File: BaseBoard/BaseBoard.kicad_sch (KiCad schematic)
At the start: 43 parts, among them J1 USB_C_DEALON-USB-US31-106, J2 Serial Port, J3 base connector, Q1 PMN48XP, SW2 boot, SW3 Reset, U1 ESP32-WROOM-E, U3 MCP73831-2ACI-OT, U4 XC6210B332MR

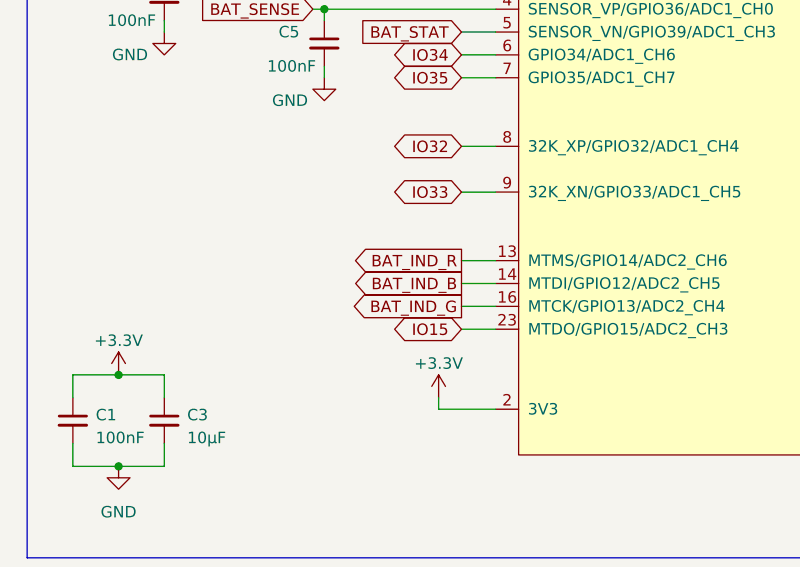
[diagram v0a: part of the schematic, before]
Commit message: Reroutes pins for the LED
After fixing the schematic symbol, we needed to reflect the changes in
the layout.
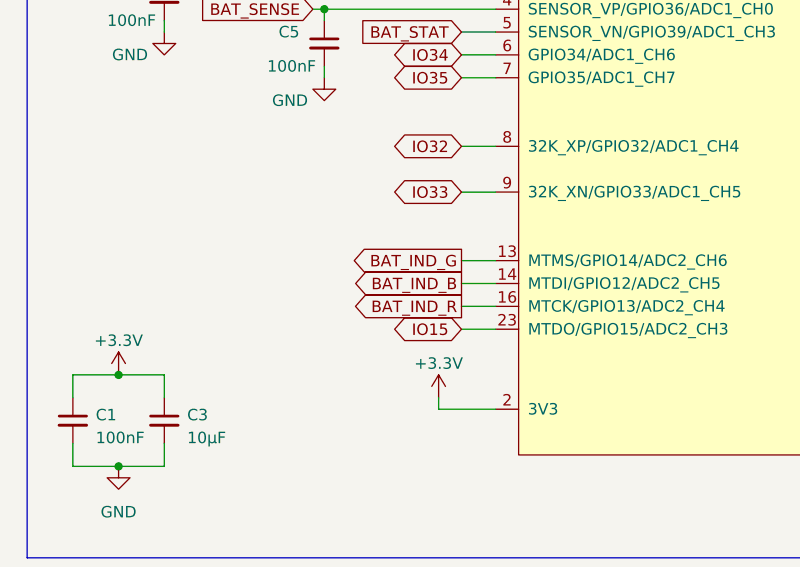
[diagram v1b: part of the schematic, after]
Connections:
- net BAT_IND_G: now also U1.13 (MTMS/GPIO14/ADC2_CH6); no longer U1.16 (MTCK/GPIO13/ADC2_CH4)
- net BAT_IND_R: now also U1.16 (MTCK/GPIO13/ADC2_CH4); no longer U1.13 (MTMS/GPIO14/ADC2_CH6)
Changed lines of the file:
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@@
     )
   )
-  (global_label "BAT_IND_R" (shape output) (at 62.23 87.63 180) (fields_autoplaced)
+  (global_label "BAT_IND_R" (shape output) (at 62.23 92.71 180) (fields_autoplaced)
     (effects (font (size 1.27 1.27)) (justify right))
-    (property "Intersheetrefs" "${INTERSHEET_REFS}" (id 0) (at 49.7463 87.63 0)
+    (property "Intersheetrefs" "${INTERSHEET_REFS}" (id 0) (at 49.7463 92.71 0)
       (effects (font (size 1.27 1.27)) (justify right) hide)
     )
@@
     )
   )
-  (global_label "BAT_IND_G" (shape output) (at 62.23 92.71 180) (fields_autoplaced)
+  (global_label "BAT_IND_G" (shape output) (at 62.23 87.63 180) (fields_autoplaced)
     (effects (font (size 1.27 1.27)) (justify right))
-    (property "Intersheetrefs" "${INTERSHEET_REFS}" (id 0) (at 49.7463 92.71 0)
+    (property "Intersheetrefs" "${INTERSHEET_REFS}" (id 0) (at 49.7463 87.63 0)
       (effects (font (size 1.27 1.27)) (justify right) hide)
     )

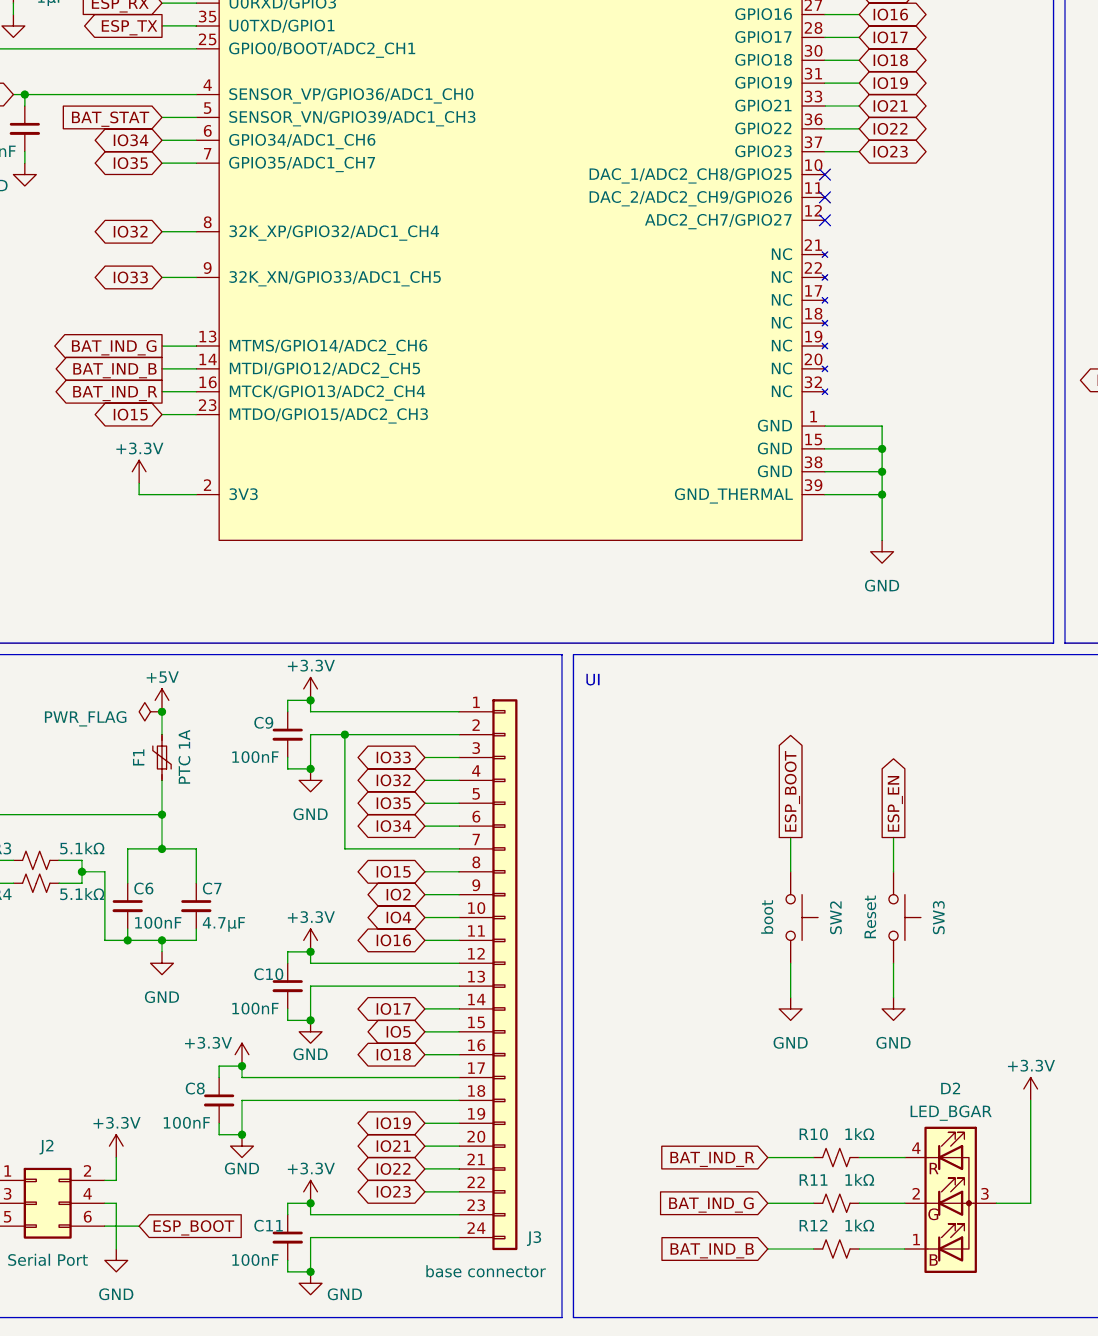
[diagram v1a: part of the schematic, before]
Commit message: Adds unused pins to the add-on connector
Those pins were used to get the ID from the DIP switches, but since we
don't have them anymore, we can use them as GPIOs.

This commit changes the connector on the baseboard (including rerouting
the traces) and updates the add-on connector schematic symbol in the
symbol library, but does not update yet the boards that use the add-on
connector (sensor board and breakout board).
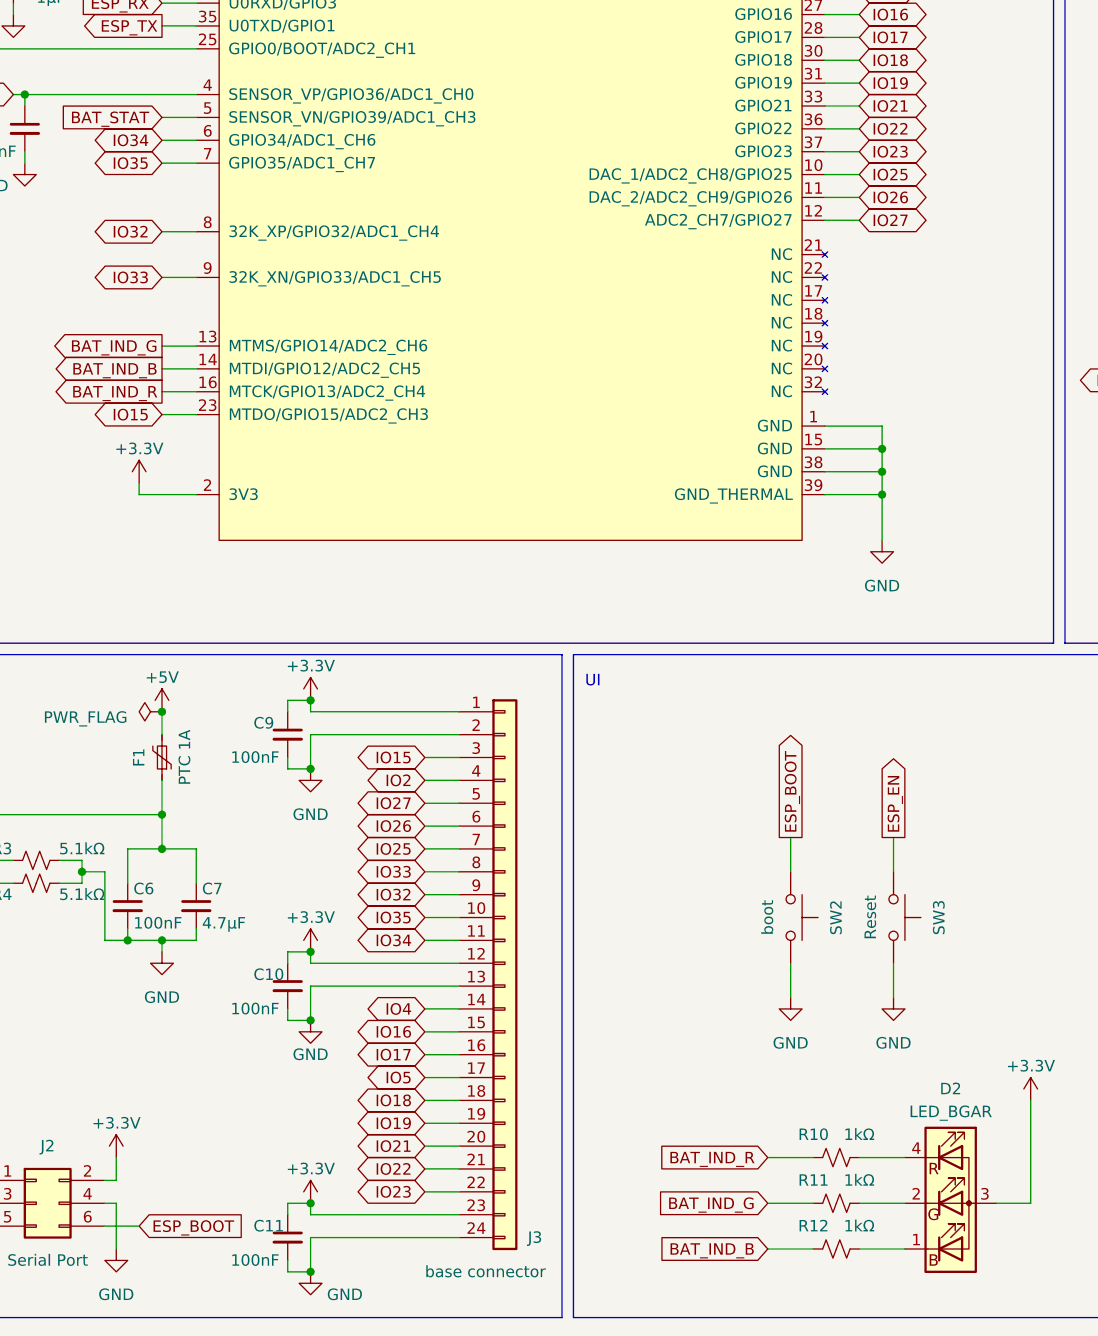
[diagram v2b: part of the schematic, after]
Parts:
- removed C8: 100nF, Capacitor_SMD:C_0805_2012Metric_Pad1.18x1.45mm_HandSolder, symbol Device:C_Small
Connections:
- net +3V3: no longer J3.17 (Pin_17)
- net GND: no longer J3.18 (Pin_18), J3.7 (Pin_7)
- net IO15: now also J3.3 (Pin_3); no longer J3.8 (Pin_8)
- net IO16: now also J3.15 (Pin_15); no longer J3.11 (Pin_11)
- net IO17: now also J3.16 (Pin_16); no longer J3.14 (Pin_14)
- net IO18: now also J3.18 (Pin_18); no longer J3.16 (Pin_16)
- net IO2: now also J3.4 (Pin_4); no longer J3.9 (Pin_9)
- net IO32: now also J3.9 (Pin_9); no longer J3.4 (Pin_4)
- net IO33: now also J3.8 (Pin_8); no longer J3.3 (Pin_3)
- net IO34: now also J3.11 (Pin_11); no longer J3.6 (Pin_6)
- net IO35: now also J3.10 (Pin_10); no longer J3.5 (Pin_5)
- net IO4: now also J3.14 (Pin_14); no longer J3.10 (Pin_10)
- net IO5: now also J3.17 (Pin_17); no longer J3.15 (Pin_15)
- net IO25: now reaches U1.10 (DAC_1/ADC2_CH8/GPIO25)
- net IO25: now also J3.7 (Pin_7)
- net IO26: now reaches U1.11 (DAC_2/ADC2_CH9/GPIO26)
- net IO26: now also J3.6 (Pin_6)
- net IO27: now reaches U1.12 (ADC2_CH7/GPIO27)
- net IO27: now also J3.5 (Pin_5)
- no-connect marks 3 -> 0

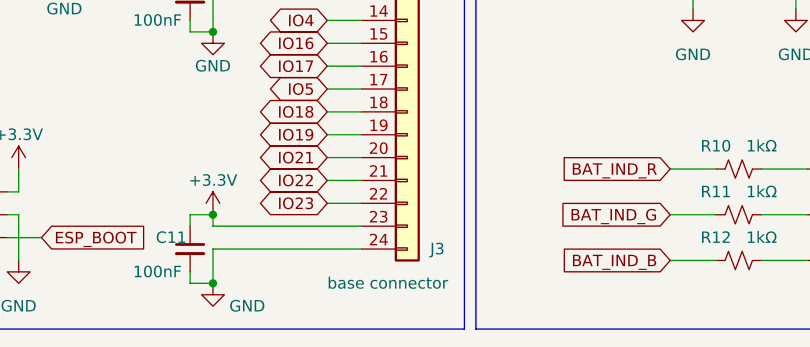
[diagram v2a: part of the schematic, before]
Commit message: Creates separate footprint for add-on and base connector
They now have marks where they need to connect together which makes it
easier on the user since they are flipped relative to each other.

I also add the 3D model for another connector. It's not correct, but I
changed my mind again about having them.
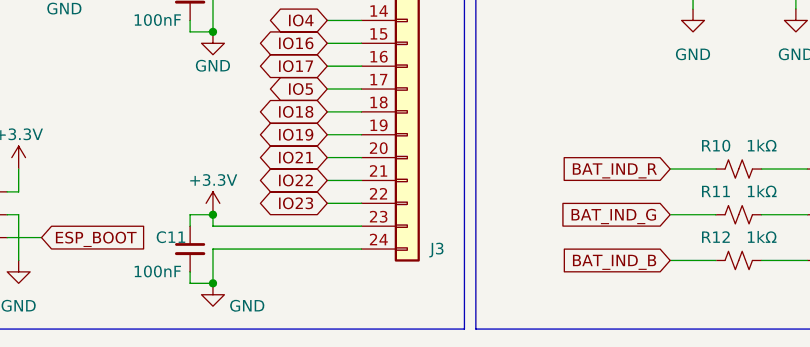
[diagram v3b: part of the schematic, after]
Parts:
- D2: footprint (none) -> GameOver:Hongzhi_Forest_HS-1204-RGB
- J3: value base connector -> (none); footprint GameOver:TXGA_FFC05036-24SBD113W5M_1x24_P0.50mm_Horizontal -> (none)

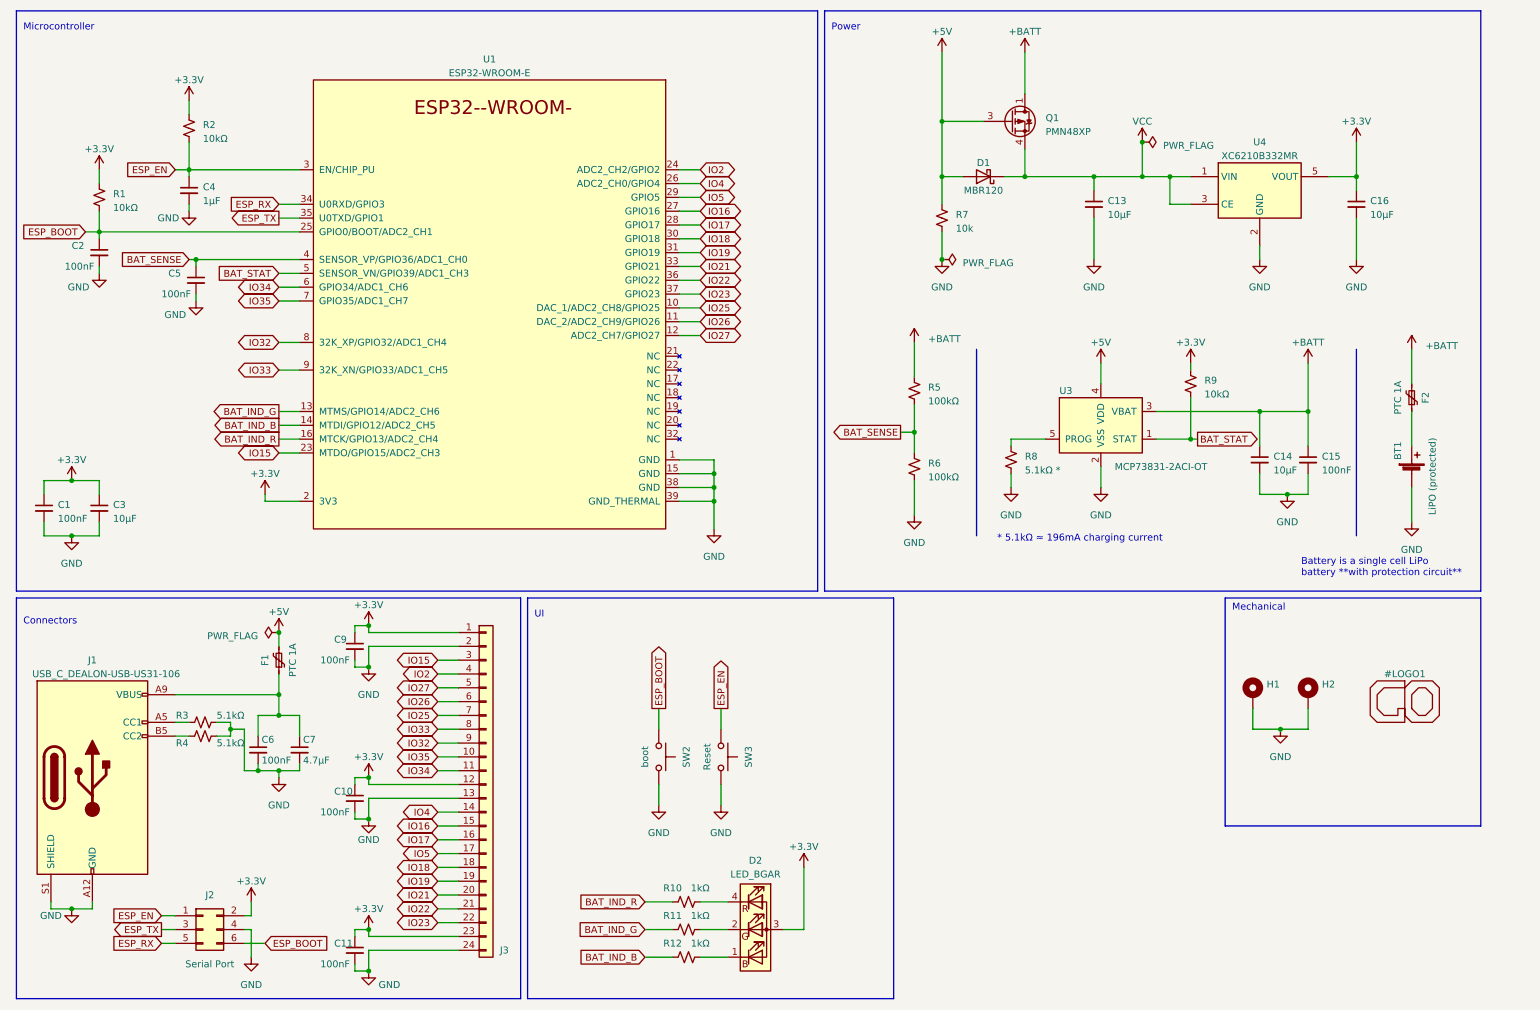
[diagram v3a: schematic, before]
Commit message: Fixes issue with battery status input
The battery status will be pulled high by the MCP73831 to it's VDD (5V)
when charging is done. This is higher than the 3.3V (+0.3V) allowed as
input to the ESP32. By adding a voltage divider we bring this to a lower
level with which we can interface to the ESP32.

When no 5V or no battery is present, the pin will be floating, so this
pin should have a internal pull-up to make sure we read the value
correctly. An internal pull-up will mean we'll see a high value with any
of charge complete, no 5V input, or no battery, which means a high value
whenever not charging.

The 150k resistor adds to the BOM, but in conjunction with the 100k it
will bring the 5V down to 3V, which is a safe value to input to the
ESP32.
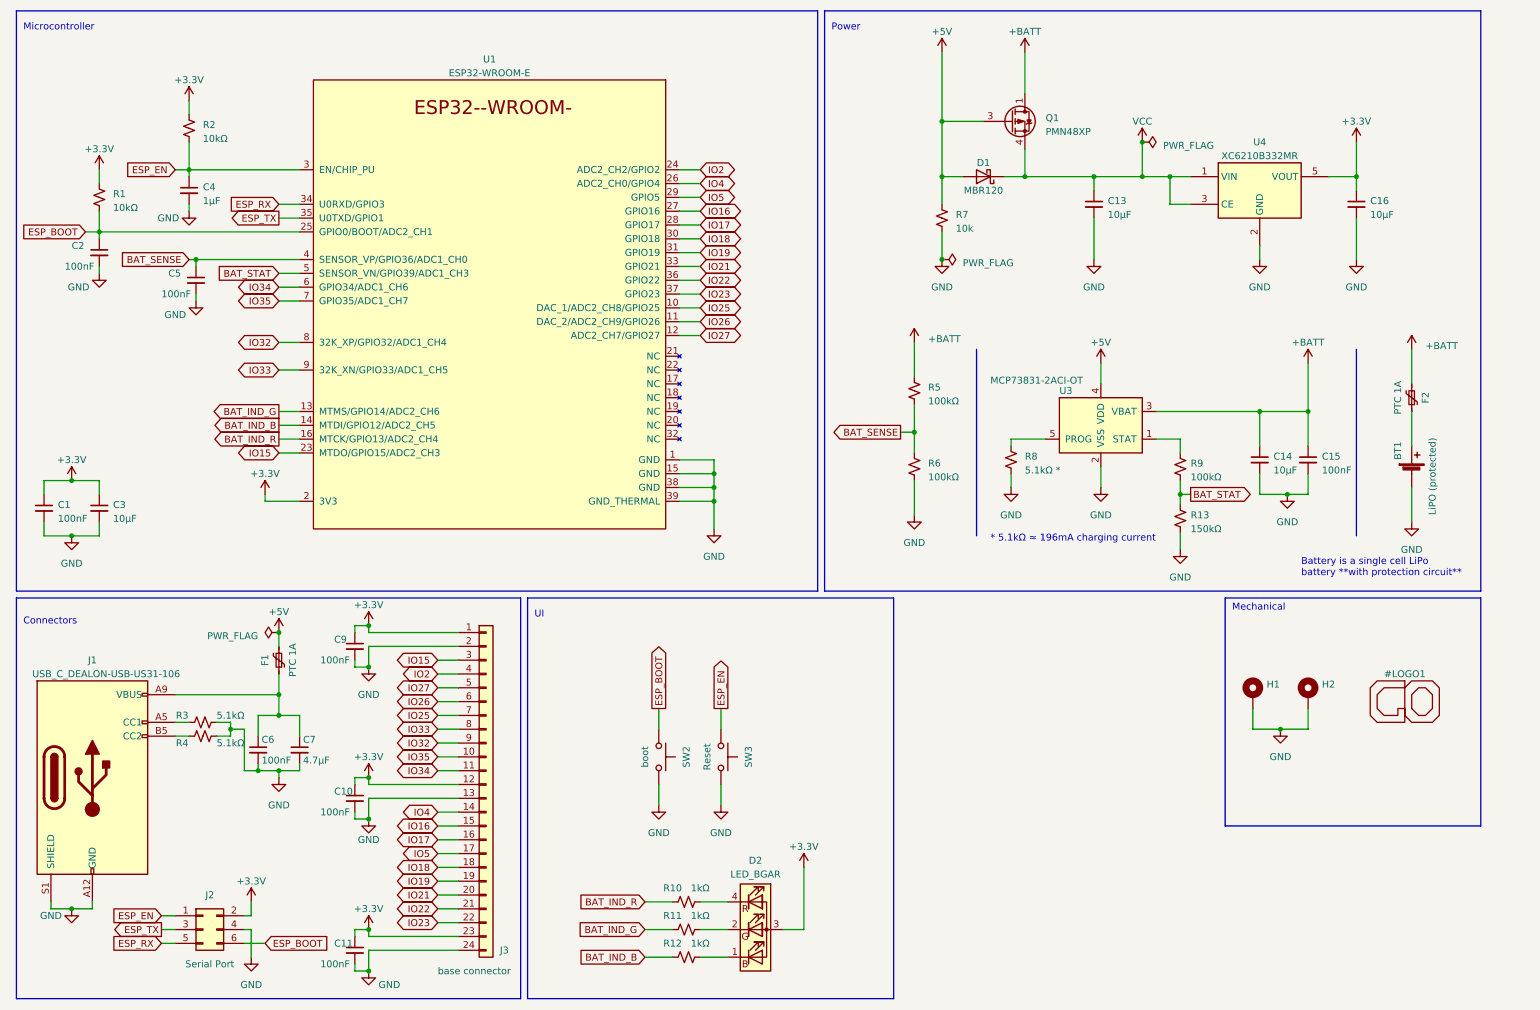
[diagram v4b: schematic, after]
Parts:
- added R13: 150kΩ, Resistor_SMD:R_0805_2012Metric_Pad1.20x1.40mm_HandSolder, symbol Device:R_Small_US
- J3: value (none) -> base connector; footprint (none) -> GameOver:Base_conn_TXGA_FFC05036-24SBD113W5M_1x24_P0.50mm_Horizontal
- R9: value 10kΩ -> 100kΩ
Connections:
- net +3V3: no longer R9.1
- net BAT_STAT: now also R13.1; no longer U3.1 (STAT)
- net GND: now also R13.2
- new net: R9.1, U3.1 (STAT)

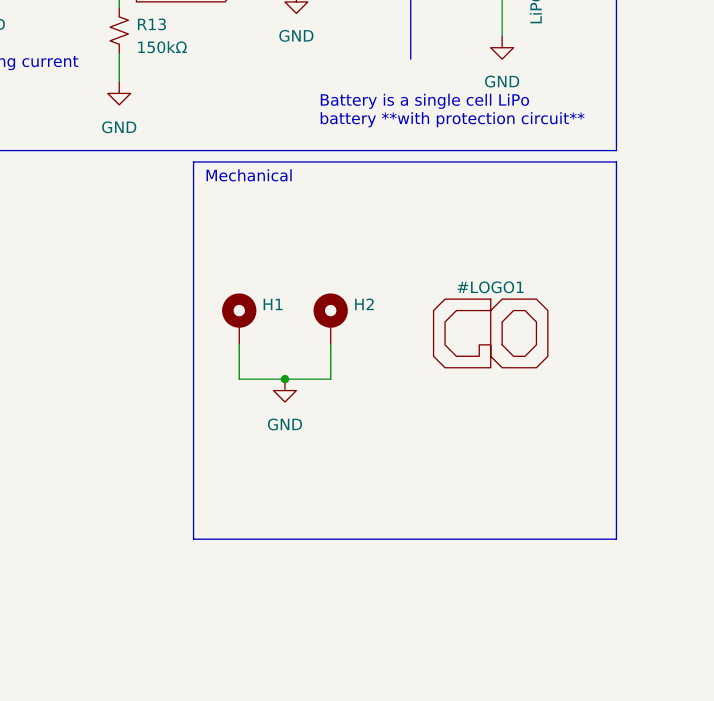
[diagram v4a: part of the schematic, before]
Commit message: Fixes logo reference so it's included in the BaseBoard.
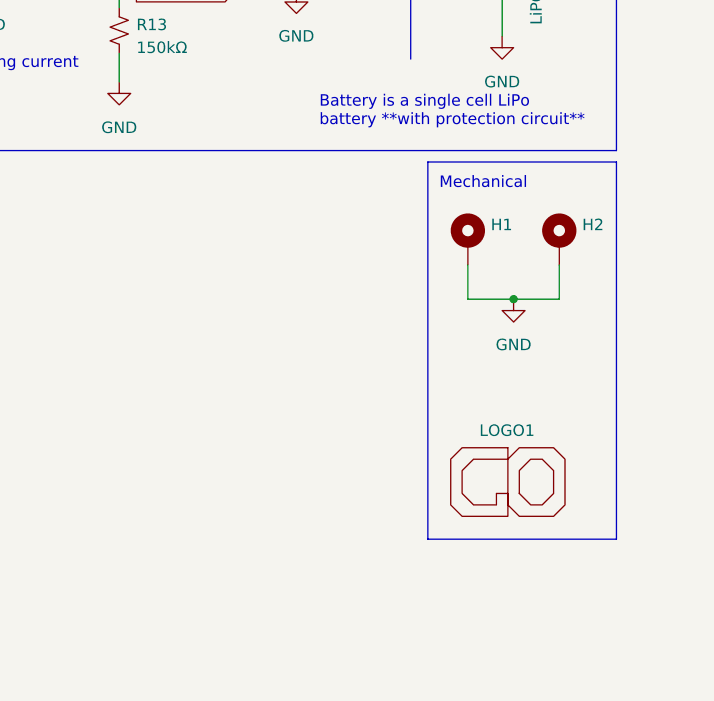
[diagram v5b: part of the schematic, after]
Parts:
- added LOGO1: (no value), symbol GameOver:GameOver_logo
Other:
- moved on the sheet: H1, H2
